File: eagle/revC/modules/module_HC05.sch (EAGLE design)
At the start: 40 parts

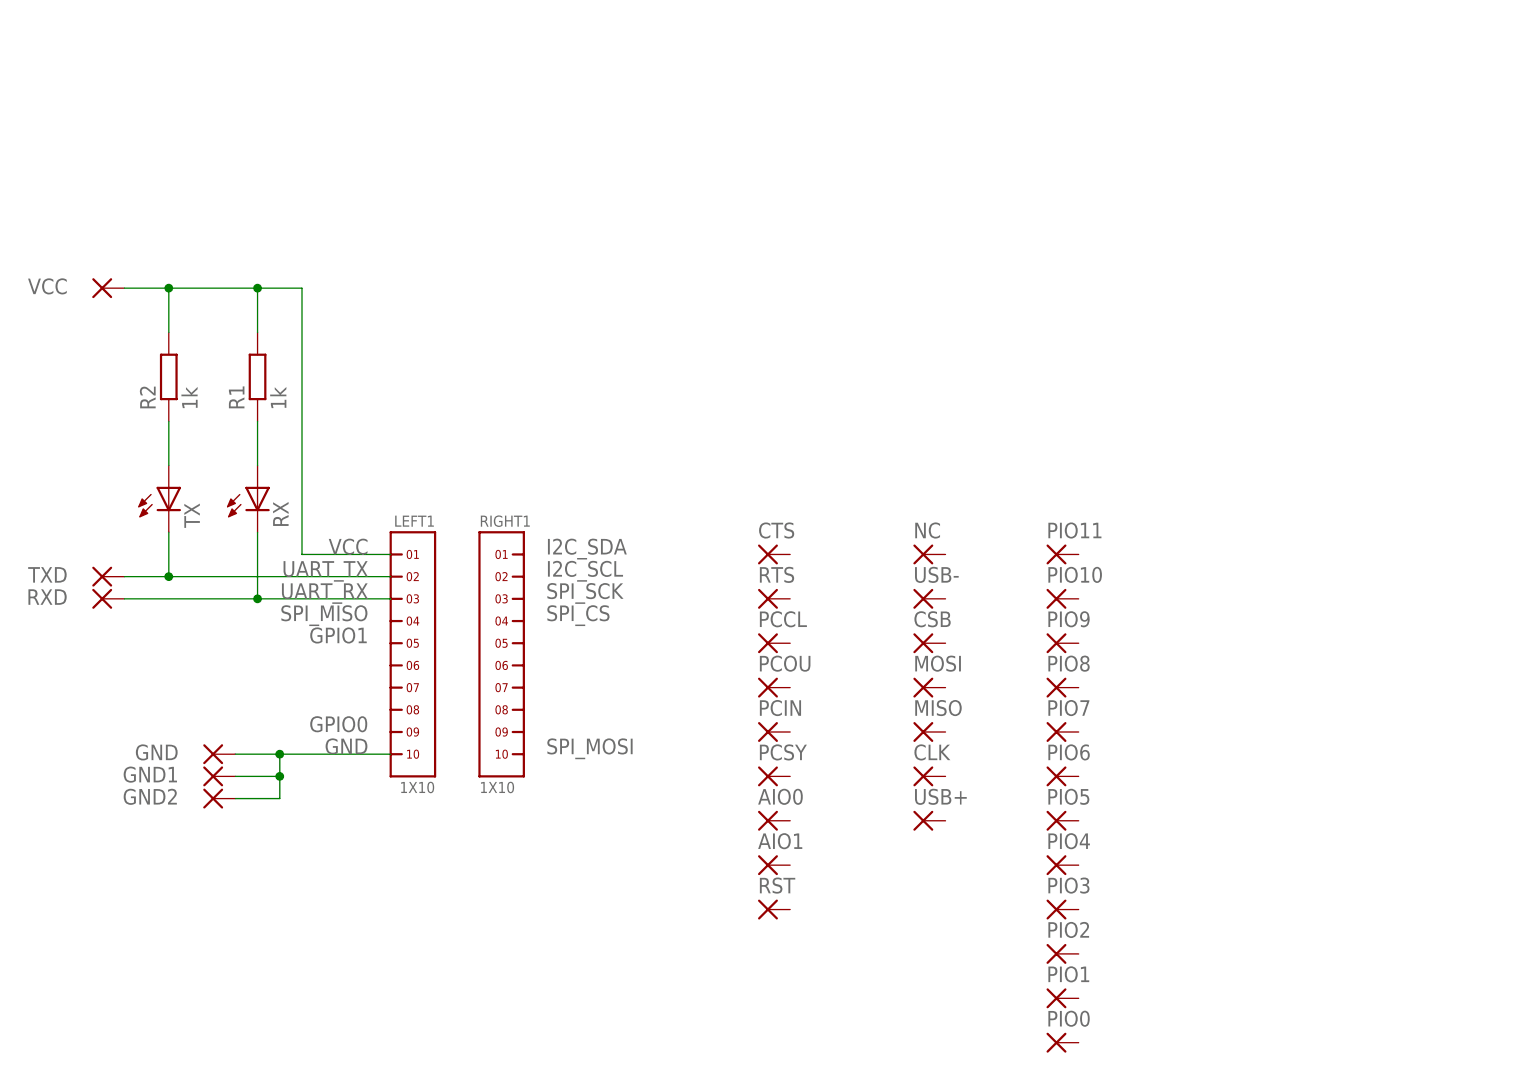
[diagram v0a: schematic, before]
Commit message: Replaced modules with library parts
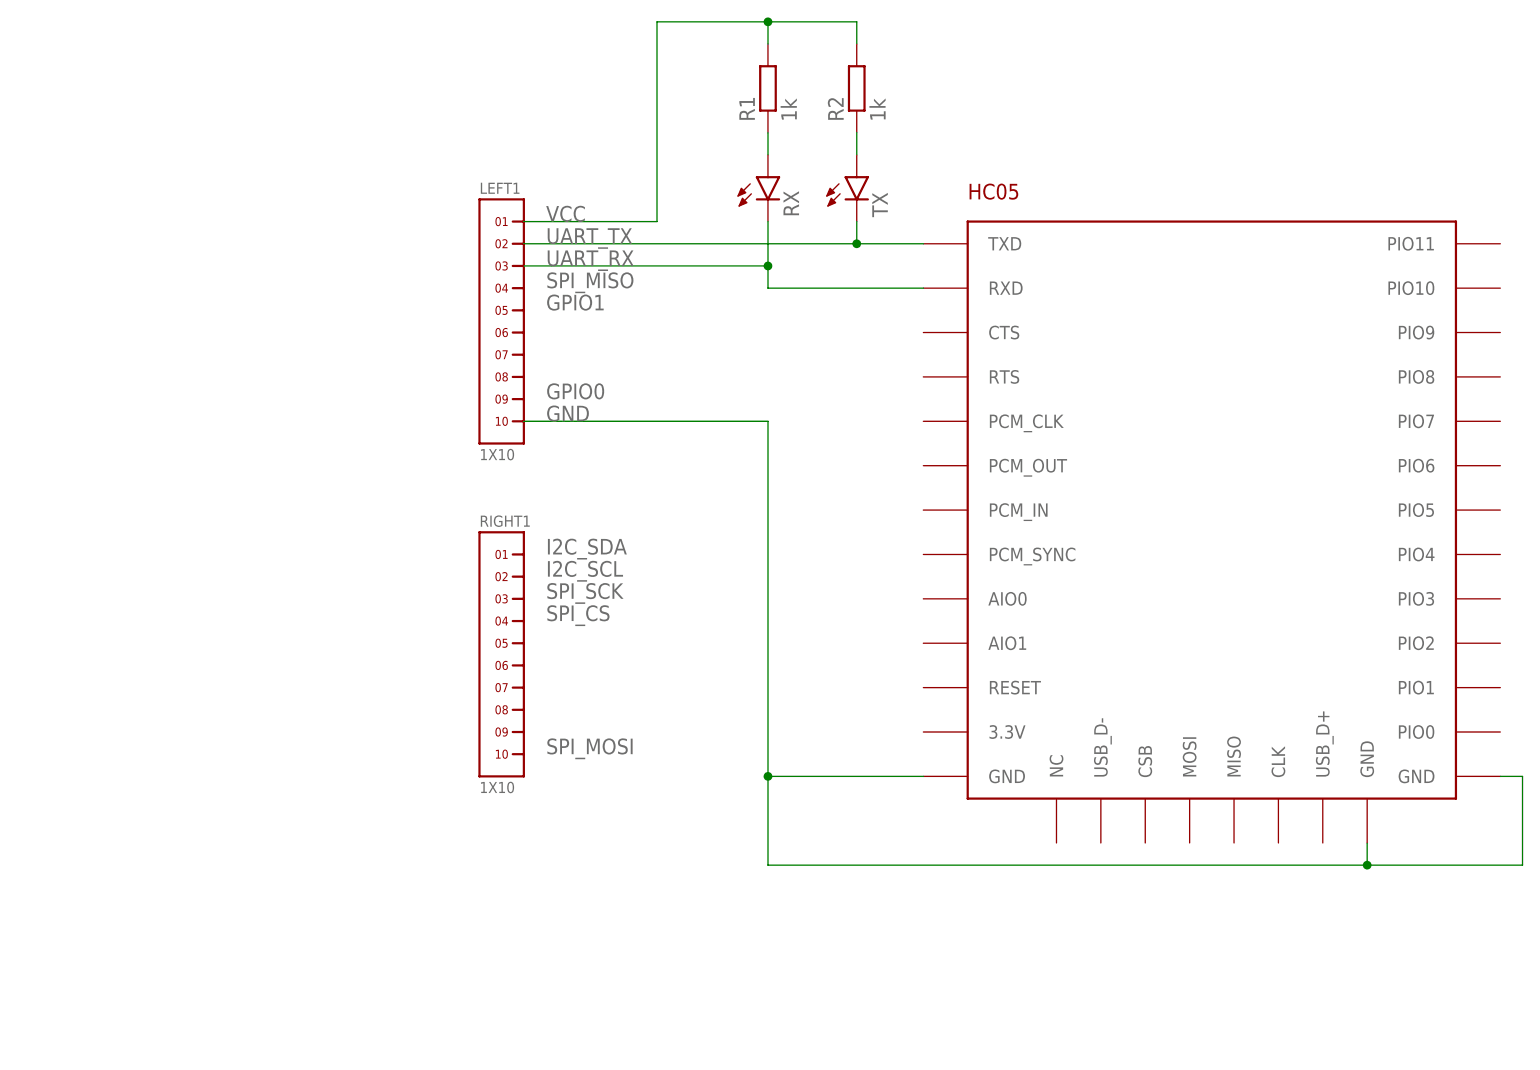
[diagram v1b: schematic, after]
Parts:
- removed AIO0, AIO1, CLK, CSB, CTS, GND, GND1, GND2, MISO, MOSI, NC, PCCL, PCIN, PCOU, PCSY, PIO0, PIO1, PIO10, PIO11, PIO2, PIO3, PIO4, PIO5, PIO6, PIO7, PIO8, PIO9, RST, RTS, RXD, TXD, USB+, USB-, VCC: (no value), wirepad:SMD1
- added U$1: HC05, RadioShield:HC05
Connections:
- removed net UART_RX: LEFT1.3, RX.C, RXD.P
- removed net UART_TX: LEFT1.2, TX.C, TXD.P
- new net N$3: LEFT1.2, TX.C, U$1.TXD
- new net N$4: LEFT1.3, RX.C, U$1.RXD
- net GND: now also U$1.GND@1, U$1.GND@2, U$1.GND@3; no longer GND.P, GND1.P, GND2.P
- net VCC: no longer VCC.P
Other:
- moved on the sheet: LEFT1, R1, R2
